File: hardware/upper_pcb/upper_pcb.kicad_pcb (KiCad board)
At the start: 2 copper layers, 54 x 54 mm, 12 parts, among them J5 FPC-6P-0.5mm, SW4 Kailh-GM8.0, SW5 Kailh-GM8.0, SW6 Alps-SKHLLBA010, SW7 Alps-SKHLLBA010

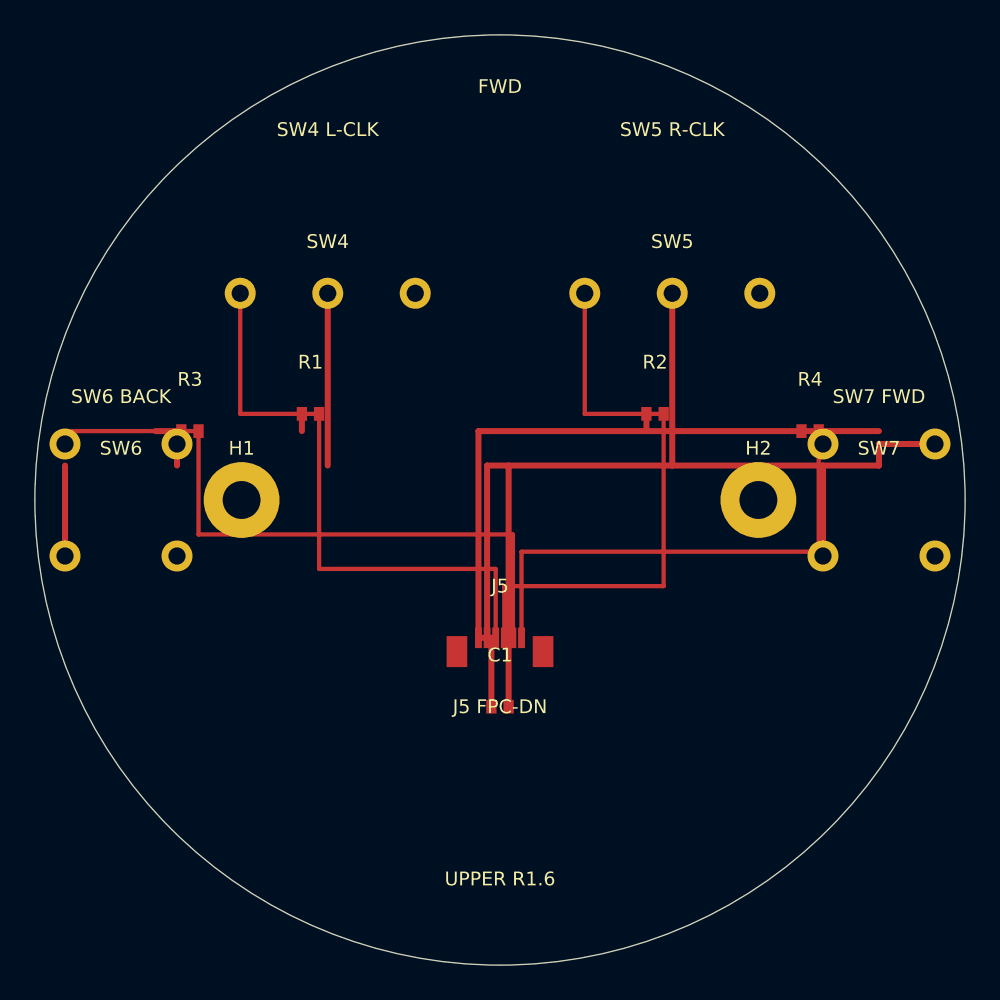
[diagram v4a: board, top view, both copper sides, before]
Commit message: feat: replace generic XIAO with Seeed XIAO ESP32-S3 (Sense) lower PCB rev 3.0
- Seeed XIAO ESP32-S3 has built-in: USB-C, 3V3 LDO (1A), LiPo charger (SGM40567),
  BOOT and RESET buttons — removed external J1 USB-C, U3 LDO, SW1 power switch
- Correct 7-pad castellated footprint: 2.54mm pitch (not 3.0mm), 1.5x2.0mm pads
- XIAO pinout per Seeed wiki: L1-L7 and R1-R7, VBAT/GND back pads
- GPIO assignments: D0-D4(left) for JOY+ADC+BTN_L; D5-D8(right) for BTN_R/BK/FW+BT_SYNC
- LiPo J2 JST-PH routes directly to XIAO VBAT back pad
- Added R_DIV1/R_DIV2 100k voltage divider for battery ADC monitoring
- Net list simplified: GND/3V3/VBAT + 9 signal nets
- Lower PCB: 370 trace segments, all F.Cu
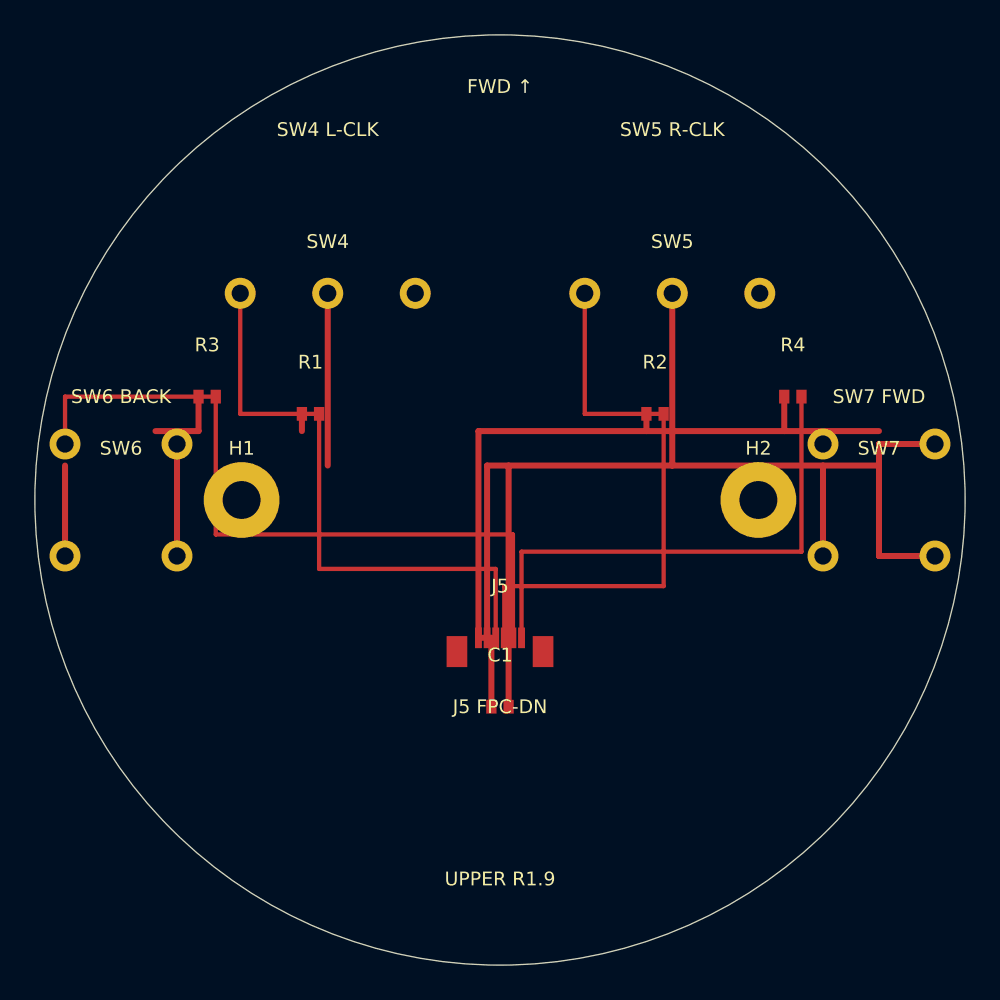
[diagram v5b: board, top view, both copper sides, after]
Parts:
- moved R3 2.24 mm to (83.0, 94.0)
- moved R4 2.24 mm to (117.0, 94.0)
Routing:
- net GND: track 83.0 -> 96.8 mm
- net 3V3: track 43.5 -> 48.5 mm
- net BTN_BK: track 38.8 -> 42.8 mm
- net BTN_FW: track 29.2 -> 30.2 mm
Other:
- board text added: "FWD ↑"
- board text added: "UPPER R1.9"
- board text removed: "FWD"
- board text removed: "UPPER R1.6"
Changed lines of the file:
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@@
   (gr_text "SW7 FWD" (at 122.0000 94.0000 0) (layer "F.SilkS") (effects (font (size 0.8 0.8) (thickness 0.15))))
   (gr_text "J5 FPC-DN" (at 100.0000 112.0000 0) (layer "F.SilkS") (effects (font (size 0.8 0.8) (thickness 0.15))))
-  (gr_text "UPPER R1.6" (at 100.0000 122.0000 0) (layer "F.SilkS") (effects (font (size 0.8 0.8) (thickness 0.15))))
-  (gr_text "FWD" (at 100.0000 76.0000 0) (layer "F.SilkS") (effects (font (size 0.8 0.8) (thickness 0.15))))
+  (gr_text "UPPER R1.9" (at 100.0000 122.0000 0) (layer "F.SilkS") (effects (font (size 0.8 0.8) (thickness 0.15))))
+  (gr_text "FWD ↑" (at 100.0000 76.0000 0) (layer "F.SilkS") (effects (font (size 0.8 0.8) (thickness 0.15))))
   (footprint "SW4" (layer "F.Cu") (at 90.0000 88.0000 0)
     (fp_text reference "SW4" (at 0 -3) (layer "F.SilkS") (effects (font (size 0.8 0.8) (thickness 0.15))))
@@
       (layers "F.Cu" "F.Mask") (net 4 "BTN_R"))
   )
-  (footprint "R3" (layer "F.Cu") (at 82.0000 96.0000 0)
+  (footprint "R3" (layer "F.Cu") (at 83.0000 94.0000 0)
     (fp_text reference "R3" (at 0 -3) (layer "F.SilkS") (effects (font (size 0.8 0.8) (thickness 0.15))))
     (fp_text value "R-0402" (at 0 3) (layer "F.Fab") hide)
@@
       (layers "F.Cu" "F.Mask") (net 5 "BTN_BK"))
   )
-  (footprint "R4" (layer "F.Cu") (at 118.0000 96.0000 0)
+  (footprint "R4" (layer "F.Cu") (at 117.0000 94.0000 0)
     (fp_text reference "R4" (at 0 -3) (layer "F.SilkS") (effects (font (size 0.8 0.8) (thickness 0.15))))
     (fp_text value "R-0402" (at 0 3) (layer "F.Fab") hide)
@@
       (drill 2.2000) (layers "*.Cu" "*.Mask") (net 1 "GND"))
   )
-# ===== COPPER TRACES (F.Cu only, all pads verified) =====
+# ===== COPPER TRACES (F.Cu, pad coords verified) =====
   (segment (start 98.7500 108.0000) (end 98.7500 96.0000) (width 0.3500) (layer "F.Cu") (net 2))
   (segment (start 98.7500 96.0000) (end 122.0000 96.0000) (width 0.3500) (layer "F.Cu") (net 2))
@@
   (segment (start 108.5000 96.0000) (end 108.5000 96.0000) (width 0.3500) (layer "F.Cu") (net 2))
   (segment (start 108.5000 96.0000) (end 108.5000 95.0000) (width 0.3500) (layer "F.Cu") (net 2))
-  (segment (start 80.0000 96.0000) (end 81.5000 96.0000) (width 0.3500) (layer "F.Cu") (net 2))
+  (segment (start 80.0000 96.0000) (end 82.5000 96.0000) (width 0.3500) (layer "F.Cu") (net 2))
+  (segment (start 82.5000 96.0000) (end 82.5000 94.0000) (width 0.3500) (layer "F.Cu") (net 2))
 (
 s
@@
 )
 )
-  (segment (start 117.5000 96.0000) (end 117.5000 96.0000) (width 0.3500) (layer "F.Cu") (net 2))
-  (segment (start 117.5000 96.0000) (end 117.5000 96.0000) (width 0.3500) (layer "F.Cu") (net 2))
+  (segment (start 116.5000 96.0000) (end 116.5000 96.0000) (width 0.3500) (layer "F.Cu") (net 2))
+  (segment (start 116.5000 96.0000) (end 116.5000 94.0000) (width 0.3500) (layer "F.Cu") (net 2))
   (segment (start 98.7500 108.0000) (end 99.5000 108.0000) (width 0.3500) (layer "F.Cu") (net 2))
   (segment (start 99.5000 108.0000) (end 99.5000 112.0000) (width 0.3500) (layer "F.Cu") (net 2))
@@
   (segment (start 74.7500 103.2500) (end 74.7500 98.0000) (width 0.3500) (layer "F.Cu") (net 1))
   (segment (start 81.2500 103.2500) (end 81.2500 103.2500) (width 0.3500) (layer "F.Cu") (net 1))
-  (segment (start 81.2500 103.2500) (end 81.2500 103.2500) (width 0.3500) (layer "F.Cu") (net 1))
+  (segment (start 81.2500 103.2500) (end 81.2500 98.0000) (width 0.3500) (layer "F.Cu") (net 1))
   (segment (start 125.2500 96.7500) (end 122.0000 96.7500) (width 0.3500) (layer "F.Cu") (net 1))
   (segment (start 122.0000 96.7500) (end 122.0000 98.0000) (width 0.3500) (layer "F.Cu") (net 1))
   (segment (start 118.7500 103.2500) (end 118.7500 103.2500) (width 0.3500) (layer "F.Cu") (net 1))
   (segment (start 118.7500 103.2500) (end 118.7500 98.0000) (width 0.3500) (layer "F.Cu") (net 1))
+  (segment (start 125.2500 103.2500) (end 122.0000 103.2500) (width 0.3500) (layer "F.Cu") (net 1))
+  (segment (start 122.0000 103.2500) (end 122.0000 98.0000) (width 0.3500) (layer "F.Cu") (net 1))
   (segment (start 100.5000 112.0000) (end 100.5000 112.0000) (width 0.3500) (layer "F.Cu") (net 1))
   (segment (start 100.5000 112.0000) (end 100.5000 98.0000) (width 0.3500) (layer "F.Cu") (net 1))
@@
   (segment (start 104.9200 95.0000) (end 104.9200 88.0000) (width 0.2500) (layer "F.Cu") (net 4))
   (segment (start 100.7500 108.0000) (end 100.7500 102.0000) (width 0.2500) (layer "F.Cu") (net 5))
-  (segment (start 100.7500 102.0000) (end 82.5000 102.0000) (width 0.2500) (layer "F.Cu") (net 5))
-  (segment (start 82.5000 102.0000) (end 82.5000 96.0000) (width 0.2500) (layer "F.Cu") (net 5))
-  (segment (start 82.5000 96.0000) (end 74.7500 96.0000) (width 0.2500) (layer "F.Cu") (net 5))
-  (segment (start 74.7500 96.0000) (end 74.7500 96.7500) (width 0.2500) (layer "F.Cu") (net 5))
+  (segment (start 100.7500 102.0000) (end 83.5000 102.0000) (width 0.2500) (layer "F.Cu") (net 5))
+  (segment (start 83.5000 102.0000) (end 83.5000 94.0000) (width 0.2500) (layer "F.Cu") (net 5))
+  (segment (start 83.5000 94.0000) (end 74.7500 94.0000) (width 0.2500) (layer "F.Cu") (net 5))
+  (segment (start 74.7500 94.0000) (end 74.7500 96.7500) (width 0.2500) (layer "F.Cu") (net 5))
   (segment (start 101.2500 108.0000) (end 101.2500 103.0000) (width 0.2500) (layer "F.Cu") (net 6))
-  (segment (start 101.2500 103.0000) (end 118.5000 103.0000) (width 0.2500) (layer "F.Cu") (net 6))
-  (segment (start 118.5000 103.0000) (end 118.5000 96.0000) (width 0.2500) (layer "F.Cu") (net 6))
+  (segment (start 101.2500 103.0000) (end 117.5000 103.0000) (width 0.2500) (layer "F.Cu") (net 6))
+  (segment (start 117.5000 103.0000) (end 117.5000 94.0000) (width 0.2500) (layer "F.Cu") (net 6))
 (
 s
@@
 1
 1
-8
+7
 .
 5
@@
 0
 9
-6
-.
-0
+4
+.
+0

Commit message: feat: remove all traces (manual routing) + shrink silk labels
- add_traces.py is now a no-op — route in KiCad manually
- Lower PCB silk: all labels 0.6mm, shortened to fit within R44mm circle
- Upper PCB silk: all labels 0.5mm, shortened to fit within R27mm circle
- No functional changes to footprints or netlist
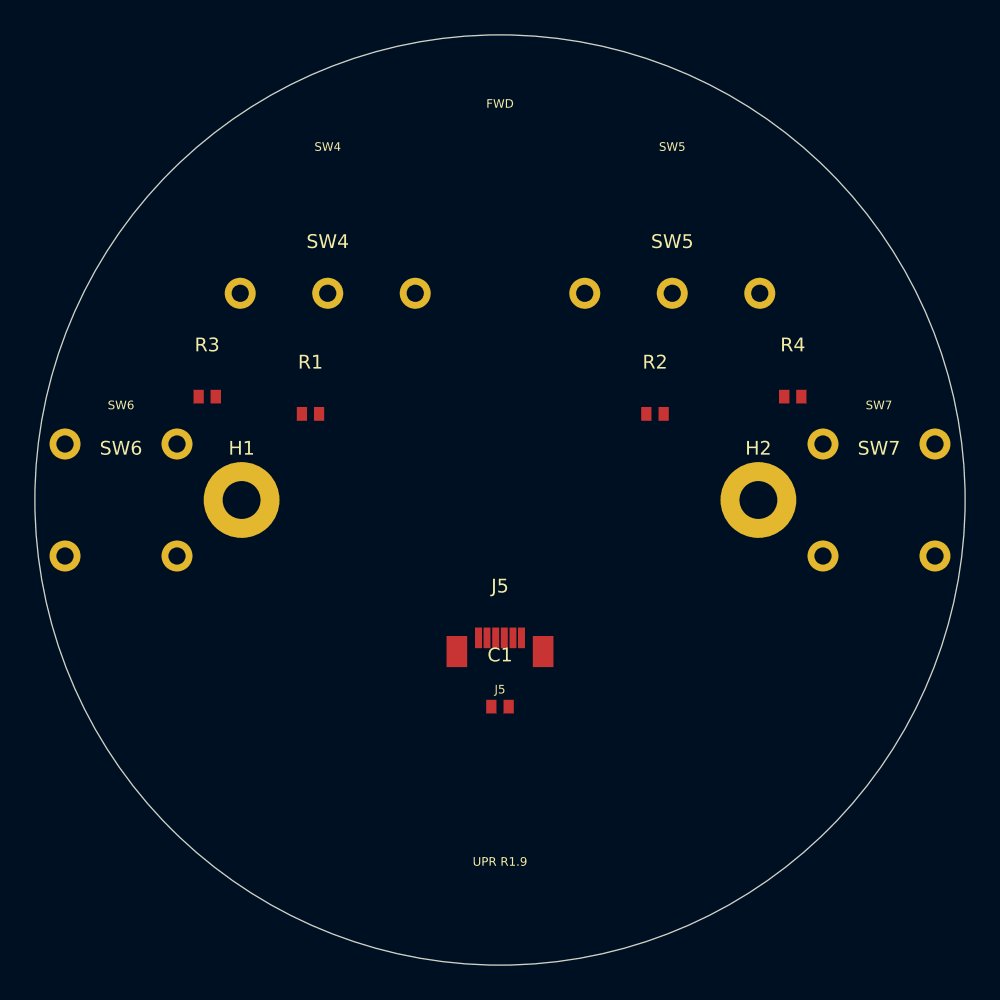
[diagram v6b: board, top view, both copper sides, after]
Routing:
- net GND: track 96.8 -> 0.00 mm
- net 3V3: track 48.5 -> 0.00 mm
- net BTN_BK: track 42.8 -> 0.00 mm
- net BTN_L: track 34.8 -> 0.00 mm
- net BTN_R: track 33.8 -> 0.00 mm
- net BTN_FW: track 30.2 -> 0.00 mm
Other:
- board text added: "FWD"
- board text added: "J5"
- board text added: "SW4"
- board text added: "SW5"
- board text added: "SW6"
- board text added: "SW7"
- board text added: "UPR R1.9"
- board text removed: "FWD ↑"
- board text removed: "J5 FPC-DN"
- board text removed: "SW4 L-CLK"
- board text removed: "SW5 R-CLK"
- board text removed: "SW6 BACK"
- board text removed: "SW7 FWD"
- board text removed: "UPPER R1.9"
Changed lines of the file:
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@@
   (net 6 "BTN_FW")
   (gr_circle (center 100.0000 100.0000) (end 127.0000 100.0000) (layer "Edge.Cuts") (width 0.050))
-  (gr_text "SW4 L-CLK" (at 90.0000 78.5000 0) (layer "F.SilkS") (effects (font (size 0.8 0.8) (thickness 0.15))))
-  (gr_text "SW5 R-CLK" (at 110.0000 78.5000 0) (layer "F.SilkS") (effects (font (size 0.8 0.8) (thickness 0.15))))
-  (gr_text "SW6 BACK" (at 78.0000 94.0000 0) (layer "F.SilkS") (effects (font (size 0.8 0.8) (thickness 0.15))))
-  (gr_text "SW7 FWD" (at 122.0000 94.0000 0) (layer "F.SilkS") (effects (font (size 0.8 0.8) (thickness 0.15))))
-  (gr_text "J5 FPC-DN" (at 100.0000 112.0000 0) (layer "F.SilkS") (effects (font (size 0.8 0.8) (thickness 0.15))))
-  (gr_text "UPPER R1.9" (at 100.0000 122.0000 0) (layer "F.SilkS") (effects (font (size 0.8 0.8) (thickness 0.15))))
-  (gr_text "FWD ↑" (at 100.0000 76.0000 0) (layer "F.SilkS") (effects (font (size 0.8 0.8) (thickness 0.15))))
+  (gr_text "SW4" (at 90.0000 79.5000 0) (layer "F.SilkS") (effects (font (size 0.5 0.5) (thickness 0.15))))
+  (gr_text "SW5" (at 110.0000 79.5000 0) (layer "F.SilkS") (effects (font (size 0.5 0.5) (thickness 0.15))))
+  (gr_text "SW6" (at 78.0000 94.5000 0) (layer "F.SilkS") (effects (font (size 0.5 0.5) (thickness 0.15))))
+  (gr_text "SW7" (at 122.0000 94.5000 0) (layer "F.SilkS") (effects (font (size 0.5 0.5) (thickness 0.15))))
+  (gr_text "J5" (at 100.0000 111.0000 0) (layer "F.SilkS") (effects (font (size 0.5 0.5) (thickness 0.15))))
+  (gr_text "UPR R1.9" (at 100.0000 121.0000 0) (layer "F.SilkS") (effects (font (size 0.5 0.5) (thickness 0.15))))
+  (gr_text "FWD" (at 100.0000 77.0000 0) (layer "F.SilkS") (effects (font (size 0.5 0.5) (thickness 0.15))))
   (footprint "SW4" (layer "F.Cu") (at 90.0000 88.0000 0)
     (fp_text reference "SW4" (at 0 -3) (layer "F.SilkS") (effects (font (size 0.8 0.8) (thickness 0.15))))
@@
       (drill 2.2000) (layers "*.Cu" "*.Mask") (net 1 "GND"))
   )
-# ===== COPPER TRACES (F.Cu, pad coords verified) =====
-  (segment (start 98.7500 108.0000) (end 98.7500 96.0000) (width 0.3500) (layer "F.Cu") (net 2))
-  (segment (start 98.7500 96.0000) (end 122.0000 96.0000) (width 0.3500) (layer "F.Cu") (net 2))
-  (segment (start 88.5000 96.0000) (end 88.5000 96.0000) (width 0.3500) (layer "F.Cu") (net 2))
-  (segment (start 88.5000 96.0000) (end 88.5000 95.0000) (width 0.3500) (layer "F.Cu") (net 2))
-  (segment (start 108.5000 96.0000) (end 108.5000 96.0000) (width 0.3500) (layer "F.Cu") (net 2))
-  (segment (start 108.5000 96.0000) (end 108.5000 95.0000) (width 0.3500) (layer "F.Cu") (net 2))
-  (segment (start 80.0000 96.0000) (end 82.5000 96.0000) (width 0.3500) (layer "F.Cu") (net 2))
-  (segment (start 82.5000 96.0000) (end 82.5000 94.0000) (width 0.3500) (layer "F.Cu") (net 2))
-(
-s
-e
-g
-m
-e
-n
-t
-(
-s
-t
-a
-r
-t
-8
-0
-.
-0
-0
-0
-0
-9
-6
-.
-0
-0
-0
-0
 )
-(
-e
-n
-d
-9
-8
-.
-7
-5
-0
-0
-9
-6
-.
-0
-0
-0
-0
-)
-(
-w
-i
-d
-t
-h
-0
-.
-3
-5
-0
-0
-)
-(
-l
-a
-y
-e
-r
-"
-F
-.
-C
-u
-"
-)
-(
-n
-e
-t
-2
-)
-)
-  (segment (start 116.5000 96.0000) (end 116.5000 96.0000) (width 0.3500) (layer "F.Cu") (net 2))
-  (segment (start 116.5000 96.0000) (end 116.5000 94.0000) (width 0.3500) (layer "F.Cu") (net 2))
-  (segment (start 98.7500 108.0000) (end 99.5000 108.0000) (width 0.3500) (layer "F.Cu") (net 2))
-  (segment (start 99.5000 108.0000) (end 99.5000 112.0000) (width 0.3500) (layer "F.Cu") (net 2))
-  (segment (start 99.2500 108.0000) (end 99.2500 98.0000) (width 0.3500) (layer "F.Cu") (net 1))
-  (segment (start 99.2500 98.0000) (end 122.0000 98.0000) (width 0.3500) (layer "F.Cu") (net 1))
-  (segment (start 90.0000 88.0000) (end 90.0000 88.0000) (width 0.3500) (layer "F.Cu") (net 1))
-  (segment (start 90.0000 88.0000) (end 90.0000 98.0000) (width 0.3500) (layer "F.Cu") (net 1))
-  (segment (start 110.0000 88.0000) (end 110.0000 88.0000) (width 0.3500) (layer "F.Cu") (net 1))
-  (segment (start 110.0000 88.0000) (end 110.0000 98.0000) (width 0.3500) (layer "F.Cu") (net 1))
-  (segment (start 81.2500 96.7500) (end 81.2500 96.7500) (width 0.3500) (layer "F.Cu") (net 1))
-  (segment (start 81.2500 96.7500) (end 81.2500 98.0000) (width 0.3500) (layer "F.Cu") (net 1))
-  (segment (start 74.7500 103.2500) (end 74.7500 103.2500) (width 0.3500) (layer "F.Cu") (net 1))
-  (segment (start 74.7500 103.2500) (end 74.7500 98.0000) (width 0.3500) (layer "F.Cu") (net 1))
-  (segment (start 81.2500 103.2500) (end 81.2500 103.2500) (width 0.3500) (layer "F.Cu") (net 1))
-  (segment (start 81.2500 103.2500) (end 81.2500 98.0000) (width 0.3500) (layer "F.Cu") (net 1))
-  (segment (start 125.2500 96.7500) (end 122.0000 96.7500) (width 0.3500) (layer "F.Cu") (net 1))
-  (segment (start 122.0000 96.7500) (end 122.0000 98.0000) (width 0.3500) (layer "F.Cu") (net 1))
-  (segment (start 118.7500 103.2500) (end 118.7500 103.2500) (width 0.3500) (layer "F.Cu") (net 1))
-  (segment (start 118.7500 103.2500) (end 118.7500 98.0000) (width 0.3500) (layer "F.Cu") (net 1))
-  (segment (start 125.2500 103.2500) (end 122.0000 103.2500) (width 0.3500) (layer "F.Cu") (net 1))
-  (segment (start 122.0000 103.2500) (end 122.0000 98.0000) (width 0.3500) (layer "F.Cu") (net 1))
-  (segment (start 100.5000 112.0000) (end 100.5000 112.0000) (width 0.3500) (layer "F.Cu") (net 1))
-  (segment (start 100.5000 112.0000) (end 100.5000 98.0000) (width 0.3500) (layer "F.Cu") (net 1))
-  (segment (start 99.7500 108.0000) (end 99.7500 104.0000) (width 0.2500) (layer "F.Cu") (net 3))
-  (segment (start 99.7500 104.0000) (end 89.5000 104.0000) (width 0.2500) (layer "F.Cu") (net 3))
-  (segment (start 89.5000 104.0000) (end 89.5000 95.0000) (width 0.2500) (layer "F.Cu") (net 3))
-  (segment (start 89.5000 95.0000) (end 84.9200 95.0000) (width 0.2500) (layer "F.Cu") (net 3))
-  (segment (start 84.9200 95.0000) (end 84.9200 88.0000) (width 0.2500) (layer "F.Cu") (net 3))
-  (segment (start 100.2500 108.0000) (end 100.2500 105.0000) (width 0.2500) (layer "F.Cu") (net 4))
-  (segment (start 100.2500 105.0000) (end 109.5000 105.0000) (width 0.2500) (layer "F.Cu") (net 4))
-  (segment (start 109.5000 105.0000) (end 109.5000 95.0000) (width 0.2500) (layer "F.Cu") (net 4))
-  (segment (start 109.5000 95.0000) (end 104.9200 95.0000) (width 0.2500) (layer "F.Cu") (net 4))
-  (segment (start 104.9200 95.0000) (end 104.9200 88.0000) (width 0.2500) (layer "F.Cu") (net 4))
-  (segment (start 100.7500 108.0000) (end 100.7500 102.0000) (width 0.2500) (layer "F.Cu") (net 5))
-  (segment (start 100.7500 102.0000) (end 83.5000 102.0000) (width 0.2500) (layer "F.Cu") (net 5))
-  (segment (start 83.5000 102.0000) (end 83.5000 94.0000) (width 0.2500) (layer "F.Cu") (net 5))
-  (segment (start 83.5000 94.0000) (end 74.7500 94.0000) (width 0.2500) (layer "F.Cu") (net 5))
-  (segment (start 74.7500 94.0000) (end 74.7500 96.7500) (width 0.2500) (layer "F.Cu") (net 5))
-  (segment (start 101.2500 108.0000) (end 101.2500 103.0000) (width 0.2500) (layer "F.Cu") (net 6))
-  (segment (start 101.2500 103.0000) (end 117.5000 103.0000) (width 0.2500) (layer "F.Cu") (net 6))
-  (segment (start 117.5000 103.0000) (end 117.5000 94.0000) (width 0.2500) (layer "F.Cu") (net 6))
-(
-s
-e
-g
-m
-e
-n
-t
-(
-s
-t
-a
-r
-t
-1
-1
-7
-.
-5
-0
-0
-0
-9
-4
-.
-0
-0
-0
-0
-)
-(
-e
-n
-d
-1
-1
-8
-.
-7
-5
-0
-0
-9
-6
-.
-7
-5
-0
-0
-)
-(
-w
-i
-d
-t
-h
-0
-.
-2
-5
-0
-0
-)
-(
-l
-a
-y
-e
-r
-"
-F
-.
-C
-u
-"
-)
-(
-n
-e
-t
-6
-)
-)
-)
